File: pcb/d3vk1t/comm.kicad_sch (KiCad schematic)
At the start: 0 parts

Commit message: [update all schematics sheets]
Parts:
- added R3: 10K, Resistor_SMD:R_0402_1005Metric, symbol Device:R_Small
- added U3: TJA1042T,118, SOIC127P600X175-8N, symbol db-can:TJA1042T,118
- added U5: MAX3485, symbol Interface_UART:MAX3485
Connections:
- new net +3.3V: R3.2
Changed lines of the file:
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@@
 (kicad_sch (version 20230121) (generator eeschema)
   (paper "A4")
+  (wire (pts (xy 116.84 83.82) (xy 116.84 86.36))
+    (stroke (width 0) (type default))
+  )
+  (symbol (lib_id "Device:R_Small") (at 116.84 88.9 180) (unit 1)
+    (in_bom yes) (on_board yes) (dnp no)
+    (property "Reference" "R3" (at 114.3 88.9 90)
+      (effects (font (size 1.27 1.27)))
+    )
+    (property "Value" "10K" (at 119.38 88.9 90)
+      (effects (font (size 1.27 1.27)))
+    )
+    (property "Footprint" "Resistor_SMD:R_0402_1005Metric" (at 116.84 88.9 0)
+      (effects (font (size 1.27 1.27)) hide)
+    )
+    (property "Datasheet" "~" (at 116.84 88.9 0)
+      (effects (font (size 1.27 1.27)) hide)
+    )
+    (pin "1")
+    (pin "2")
+    (instances
+      (project "d3vk1t"
+        (path "/4ea523ae-7c45-478e-a9cc-6f4833d1a9d5/41f8e312-86c0-4917-8944-524577576fad"
+          (reference "R3") (unit 1)
+        )
+        (path "/4ea523ae-7c45-478e-a9cc-6f4833d1a9d5/ee5fa9de-078f-4c07-8a01-b202c218757d"
+          (reference "R14") (unit 1)
+        )
+      )
+    )
+  )
+  (symbol (lib_id "Interface_UART:MAX3485") (at 139.7 114.3 0) (unit 1)
+    (in_bom yes) (on_board yes) (dnp no) (fields_autoplaced)
+    (property "Reference" "U5" (at 141.6559 100.33 0)
+      (effects (font (size 1.27 1.27)) (justify left))
+    )
+    (property "Value" "MAX3485" (at 141.6559 102.87 0)
+      (effects (font (size 1.27 1.27)) (justify left))
+    )
+    (property "Footprint" "" (at 139.7 132.08 0)
+      (effects (font (size 1.27 1.27)) hide)
+    )
+    (property "Datasheet" "https://datasheets.maximintegrated.com/en/ds/MAX3483-MAX3491.pdf" (at 139.7 113.03 0)
+      (effects (font (size 1.27 1.27)) hide)
+    )
+    (pin "1")
+    (pin "2")
+    (pin "3")
+    (pin "4")
+    (pin "5")
+    (pin "6")
+    (pin "7")
+    (pin "8")
+    (instances
+      (project "d3vk1t"
+        (path "/4ea523ae-7c45-478e-a9cc-6f4833d1a9d5/ee5fa9de-078f-4c07-8a01-b202c218757d"
+          (reference "U5") (unit 1)
+        )
+      )
+    )
+  )
+  (symbol (lib_id "db-can:TJA1042T,118") (at 139.7 73.66 0) (unit 1)
+    (in_bom yes) (on_board yes) (dnp no) (fields_autoplaced)
+    (property "Reference" "U3" (at 139.7 57.15 0)
+      (effects (font (size 1.27 1.27)))
+    )
+    (property "Value" "TJA1042T,118" (at 139.7 59.69 0)
+      (effects (font (size 1.27 1.27)))
+    )
+    (property "Footprint" "SOIC127P600X175-8N" (at 139.7 73.66 0)
+      (effects (font (size 1.27 1.27)) (justify bottom) hide)
+    )
+    (property "Datasheet" "" (at 139.7 73.66 0)
+      (effects (font (size 1.27 1.27)) hide)
+    )
+    (property "PARTREV" "10" (at 139.7 73.66 0)
+      (effects (font (size 1.27 1.27)) (justify bottom) hide)
+    )
+    (property "MANUFACTURER" "NXP" (at 139.7 73.66 0)
+      (effects (font (size 1.27 1.27)) (justify bottom) hide)
+    )
+    (property "MAXIMUM_PACKAGE_HEIGHT" "1.75mm" (at 139.7 73.66 0)
+      (effects (font (size 1.27 1.27)) (justify bottom) hide)
+    )
+    (property "SNAPEDA_PN" "TJA1042T,118" (at 139.7 73.66 0)
+      (effects (font (size 1.27 1.27)) (justify bottom) hide)
+    )
+    (property "STANDARD" "IPC-7351B" (at 139.7 73.66 0)
+      (effects (font (size 1.27 1.27)) (justify bottom) hide)
+    )
+    (pin "1")
+    (pin "2")
+    (pin "3")
+    (pin "4")
+    (pin "5")
+    (pin "6")
+    (pin "7")
+    (pin "8")
+    (instances
+      (project "d3vk1t"
+        (path "/4ea523ae-7c45-478e-a9cc-6f4833d1a9d5/ee5fa9de-078f-4c07-8a01-b202c218757d"
+          (reference "U3") (unit 1)
+        )
+      )
+    )
+  )
+  (symbol (lib_id "power:+3.3V") (at 116.84 83.82 0) (unit 1)
+    (in_bom yes) (on_board yes) (dnp no) (fields_autoplaced)
+    (property "Reference" "#PWR02" (at 116.84 87.63 0)
+      (effects (font (size 1.27 1.27)) hide)
+    )
+    (property "Value" "+3.3V" (at 116.84 80.01 0)
+      (effects (font (size 1.27 1.27)))
+    )
+    (property "Footprint" "" (at 116.84 83.82 0)
+      (effects (font (size 1.27 1.27)) hide)
+    )
+    (property "Datasheet" "" (at 116.84 83.82 0)
+      (effects (font (size 1.27 1.27)) hide)
+    )
+    (pin "1")
+    (instances
+      (project "d3vk1t"
+        (path "/4ea523ae-7c45-478e-a9cc-6f4833d1a9d5/0c7e2350-c710-4f8b-bffc-99ae7438d4de"
+          (reference "#PWR02") (unit 1)
+        )
+        (path "/4ea523ae-7c45-478e-a9cc-6f4833d1a9d5/41f8e312-86c0-4917-8944-524577576fad"
+          (reference "#PWR012") (unit 1)
+        )
+        (path "/4ea523ae-7c45-478e-a9cc-6f4833d1a9d5/ee5fa9de-078f-4c07-8a01-b202c218757d"
+          (reference "#PWR049") (unit 1)
+        )
+      )
+    )
+  )
 )

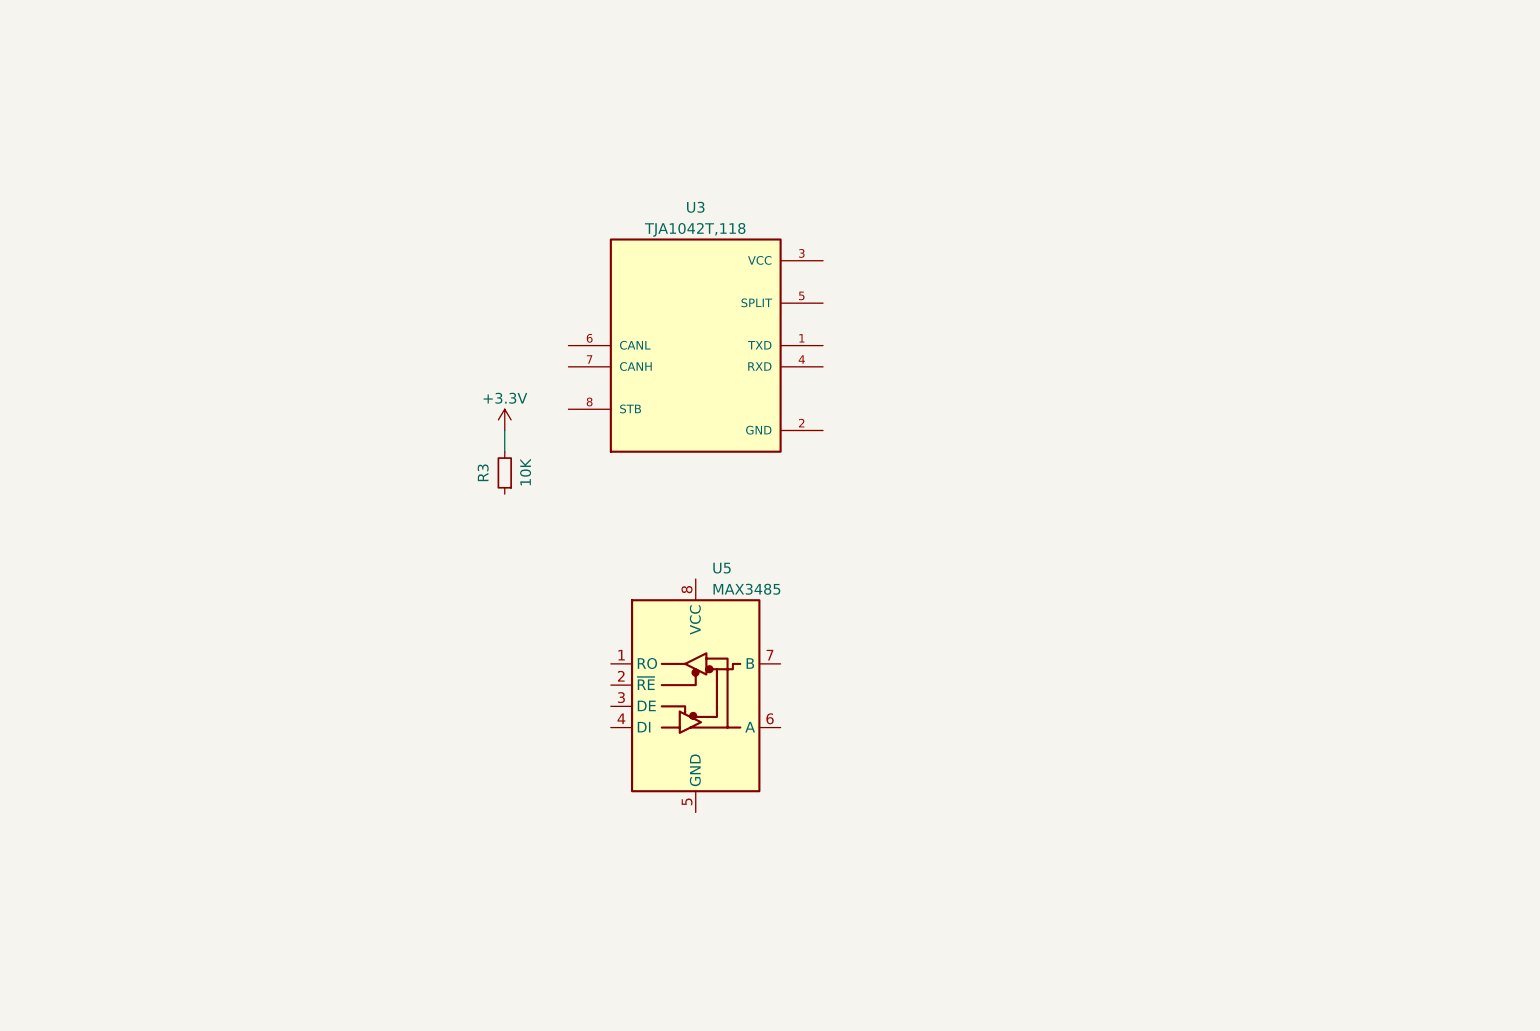
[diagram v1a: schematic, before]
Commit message: sch: update all sch sheets.
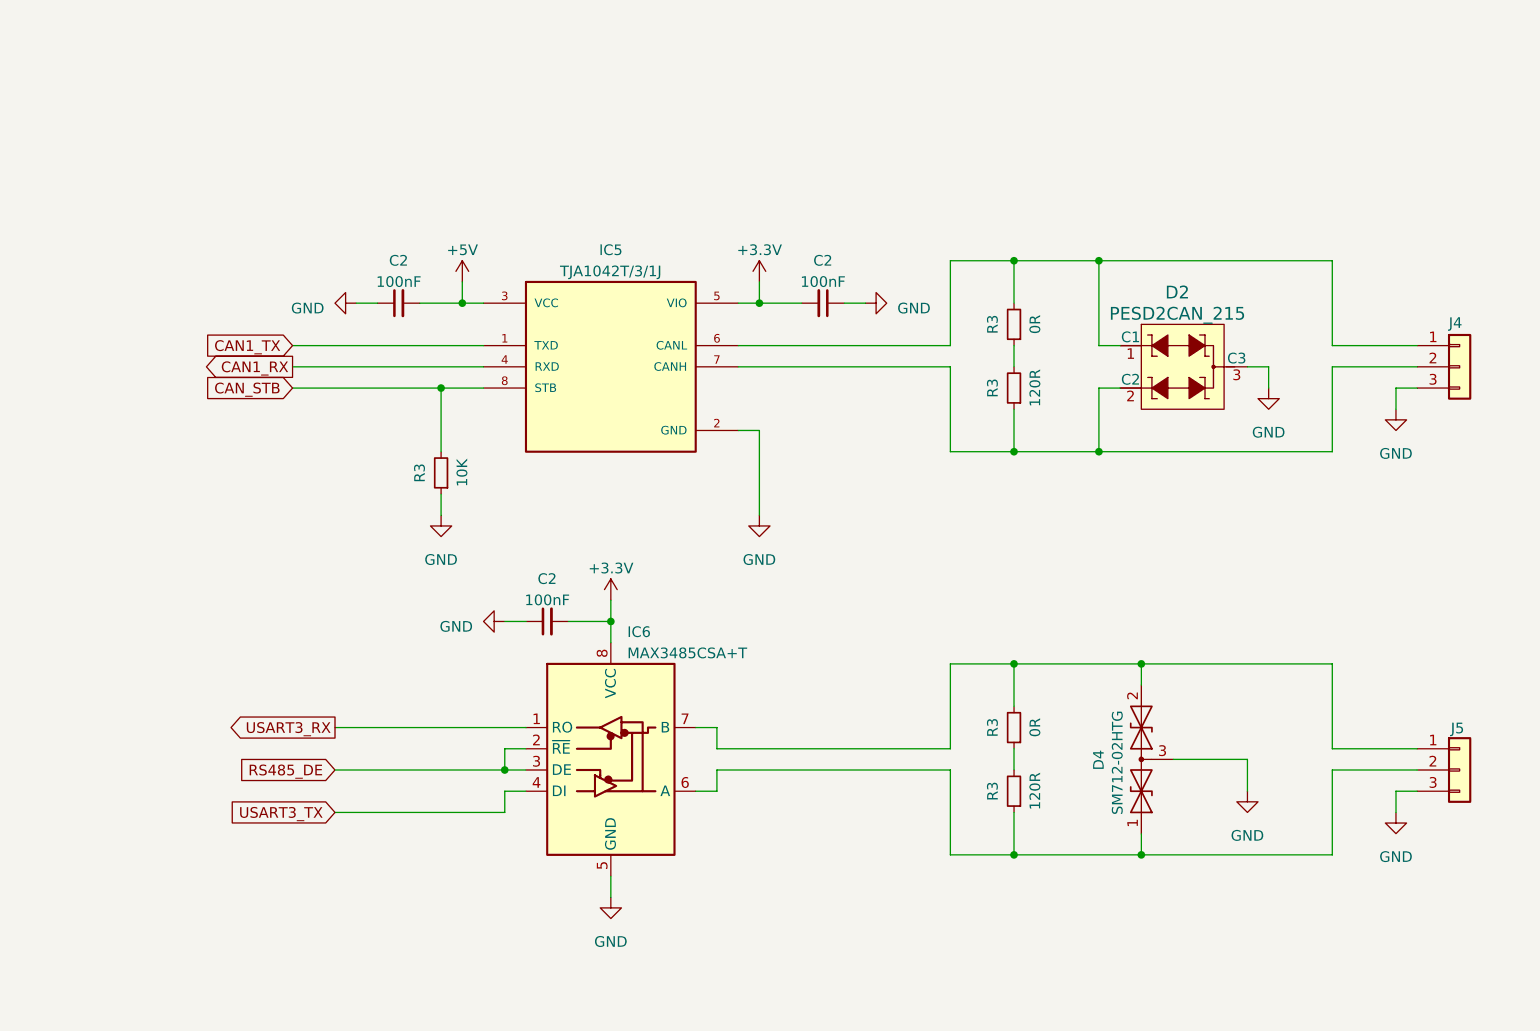
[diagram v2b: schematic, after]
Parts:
- removed U3: TJA1042T,118, SOIC127P600X175-8N, symbol db-can:TJA1042T,118
- added C2 (x3): 100nF, Capacitor_SMD:C_0402_1005Metric, symbol Device:C_Small
- added D2: PESD2CAN_215, digikey-footprints:SOT-23-3, symbol dk_TVS-Diodes:PESD2CAN_215
- added D4: SM712-02HTG, Package_TO_SOT_SMD:SOT-23, symbol Diode:SM712_SOT23
- added IC5: TJA1042T/3/1J, db:SOIC127P600X175-8N, symbol db-can:TJA1042T,118
- added J4, J5: Conn_01x03, Connector_JST:JST_XH_B3B-XH-A_1x03_P2.50mm_Vertical, symbol Connector_Generic:Conn_01x03
- added R3 (x2): 120R, Resistor_SMD:R_0402_1005Metric, symbol Device:R_Small
- added R3 (x2): 0R, Resistor_SMD:R_0402_1005Metric, symbol Device:R_Small
- IC6: renamed from U5; value MAX3485 -> MAX3485CSA+T; footprint (none) -> Package_SO:SOIC-8W_5.3x5.3mm_P1.27mm
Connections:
- net +3.3V: now also IC6.8 (VCC), C2.2, C2.2, IC5.5 (VIO); no longer R3.2
- net GND: now reaches R3.1
- net GND: now also IC6.5 (GND), C2.1, C2.1, C2.1, D2.3 (C3), D4.3 (common), IC5.2 (GND), J4.3 (Pin_3), J5.3 (Pin_3)
- net USART3_RX: now reaches IC6.1 (RO)
- net RS485_DE: now reaches IC6.2 (~{RE})
- net RS485_DE: now also IC6.3 (DE)
- net USART3_TX: now reaches IC6.4 (DI)
- net at IC6.6 (A): now also D4.1 (A1), J5.2 (Pin_2), R3.1
- net at IC6.7 (B): now also D4.2 (A2), J5.1 (Pin_1), R3.2
- new net: D2.2 (C2), IC5.7 (CANH), J4.2 (Pin_2), R3.1
- new net: R3.1, R3.2 (x2)
- new net: D2.1 (C1), IC5.6 (CANL), J4.1 (Pin_1), R3.2
- new net +5V: C2.2, IC5.3 (VCC)
- new net CAN1_RX: IC5.4 (RXD)
- new net CAN1_TX: IC5.1 (TXD)
- new net CAN_STB: IC5.8 (STB), R3.2
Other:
- moved on the sheet: IC6, R3
